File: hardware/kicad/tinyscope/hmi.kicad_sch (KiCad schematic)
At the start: 51 parts, among them J8 Waveshare 16498

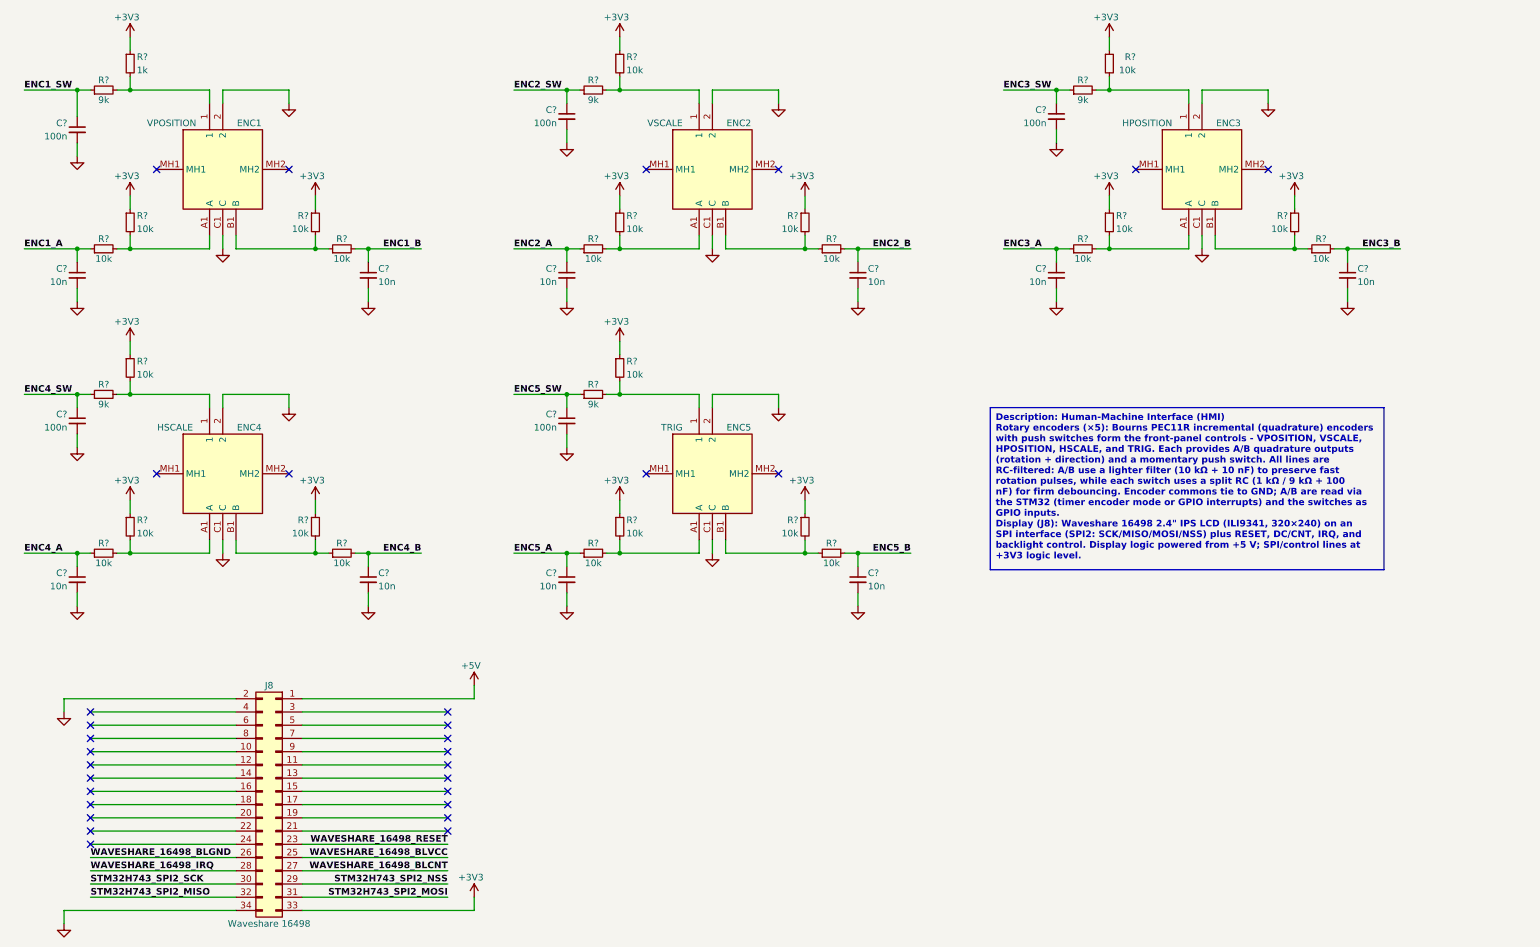
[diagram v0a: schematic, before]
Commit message: feat: hardware: Adds 6th encoder for display
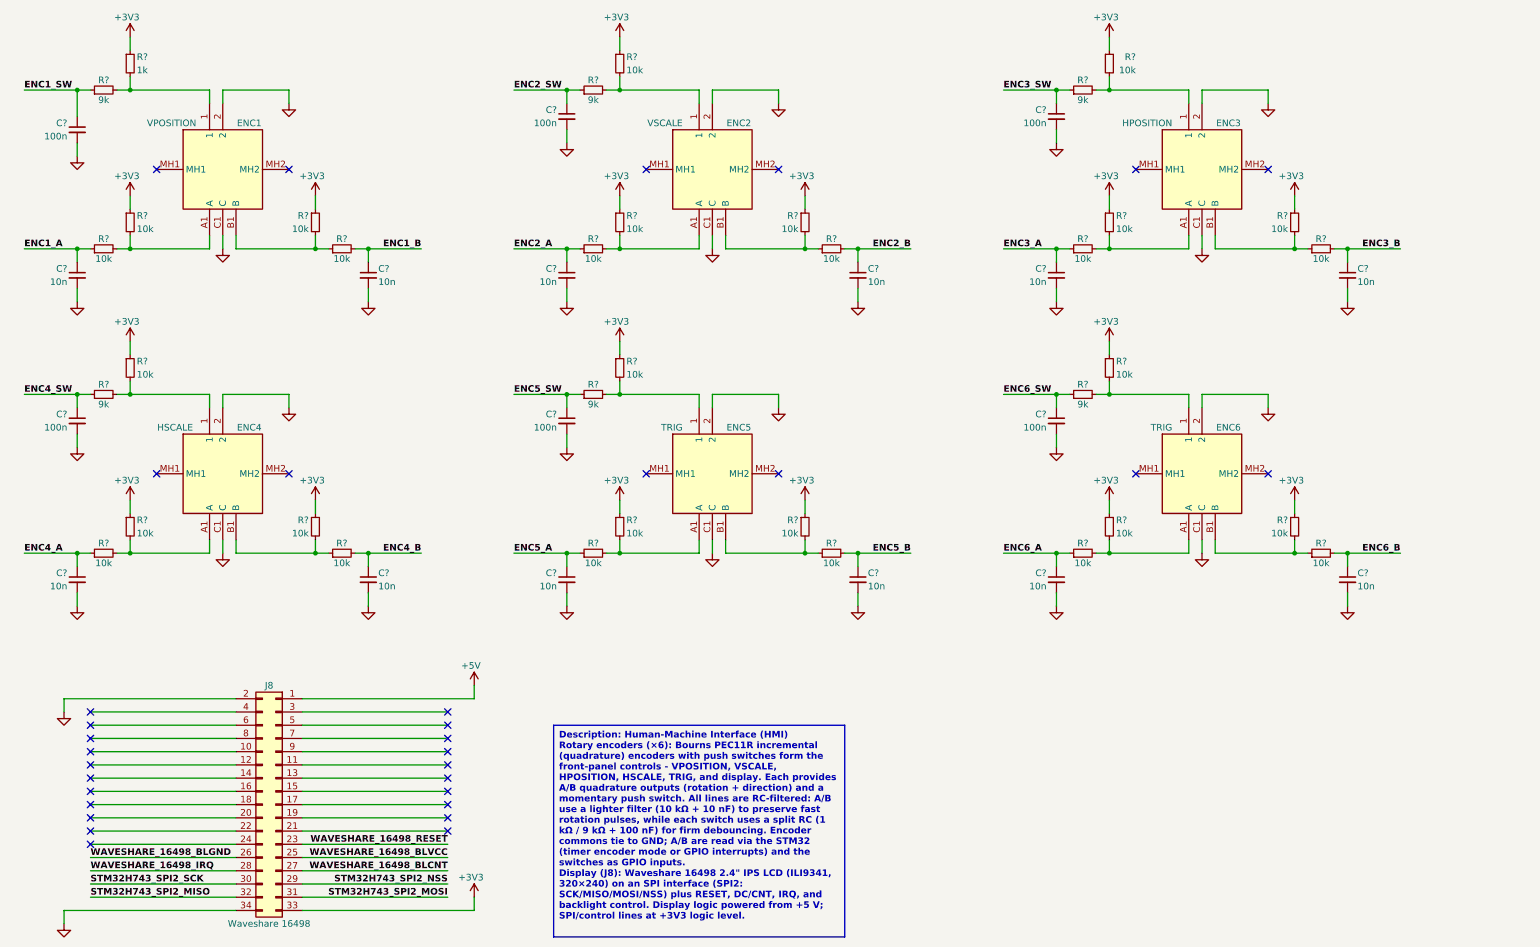
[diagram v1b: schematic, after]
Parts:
- added C?: 100n, symbol Device:C_Small
- added C? (x2): 10n, symbol Device:C_Small
- added ENC6: TRIG, PEC11R4220FS0024, symbol PEC11R-4220F-S0024:PEC11R-4220F-S0024
- added R? (x5): 10k, symbol Device:R_Small
- added R?: 9k, symbol Device:R_Small
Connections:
- net +3V3: now also R?.1, R?.1, R?.1
- net GND: now also C?.2, C?.2, C?.2, ENC6.2, ENC6.C1 (C)
- new net: ENC6.1, R?.2, R?.2
- new net: ENC6.A1 (A), R?.2, R?.2
- new net: ENC6.B1 (B), R?.1, R?.2
- new net ENC6_A: C?.1, R?.1
- new net ENC6_B: C?.1, R?.2
- new net ENC6_SW: C?.1, R?.1
- no-connect marks 31 -> 33

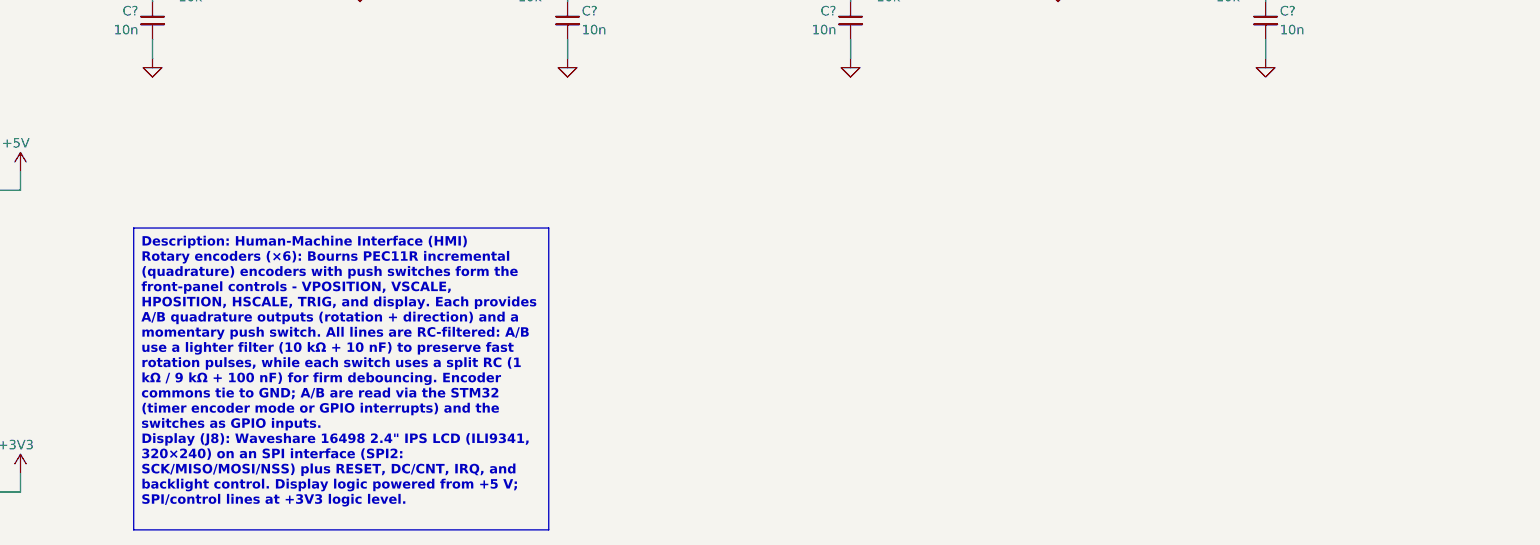
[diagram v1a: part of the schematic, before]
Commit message: feat: hardware: doc: Modifies placement for the schematic description
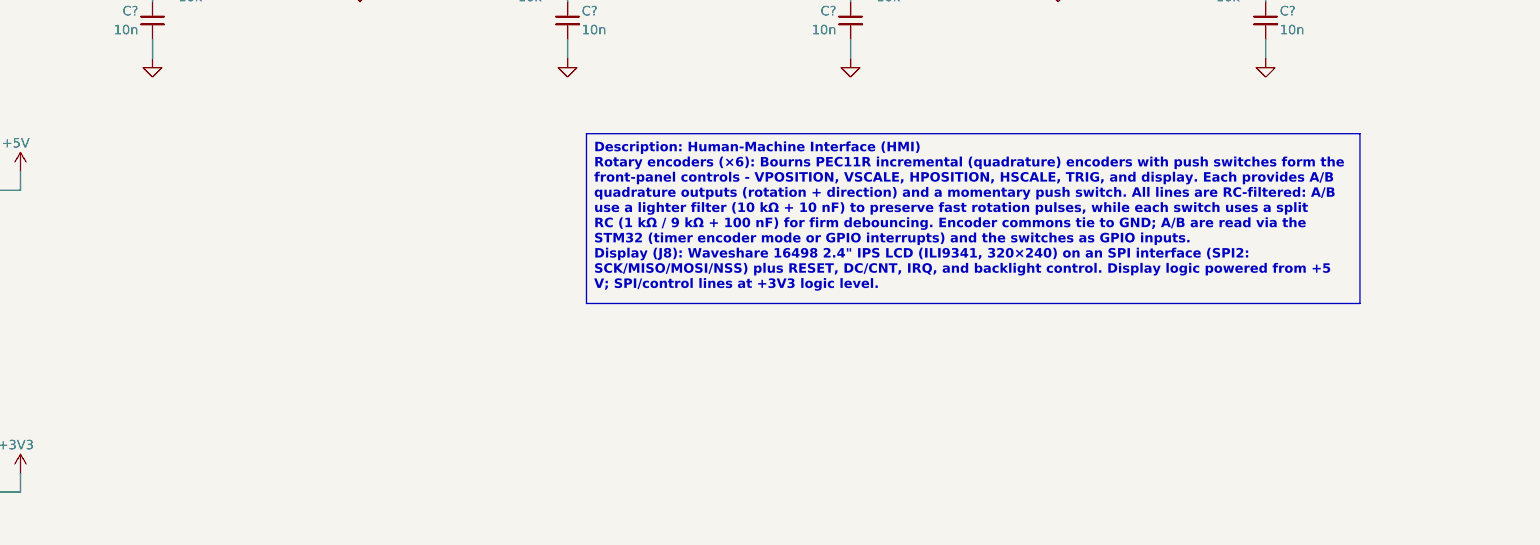
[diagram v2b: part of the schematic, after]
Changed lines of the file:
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@@
   )
   (text_box "Description: Human-Machine Interface (HMI)\nRotary encoders (×6): Bourns PEC11R incremental (quadrature) encoders with push switches form the front-panel controls - VPOSITION, VSCALE, HPOSITION, HSCALE, TRIG, and display. Each provides A/B quadrature outputs (rotation + direction) and a momentary push switch. All lines are RC-filtered: A/B use a lighter filter (10 kΩ + 10 nF) to preserve fast rotation pulses, while each switch uses a split RC (1 kΩ / 9 kΩ + 100 nF) for firm debouncing. Encoder commons tie to GND; A/B are read via the STM32 (timer encoder mode or GPIO interrupts) and the switches as GPIO inputs.\nDisplay (J8): Waveshare 16498 2.4\" IPS LCD (ILI9341, 320×240) on an SPI interface (SPI2: SCK/MISO/MOSI/NSS) plus RESET, DC/CNT, IRQ, and backlight control. Display logic powered from +5 V; SPI/control lines at +3V3 logic level."
-    (at 116.84 152.4 0) (size 55.88 40.64)
+    (at 177.8 139.7 0) (size 104.14 22.86)
     (stroke (width 0) (type default))
     (fill (type color) (color 255 255 194 1))

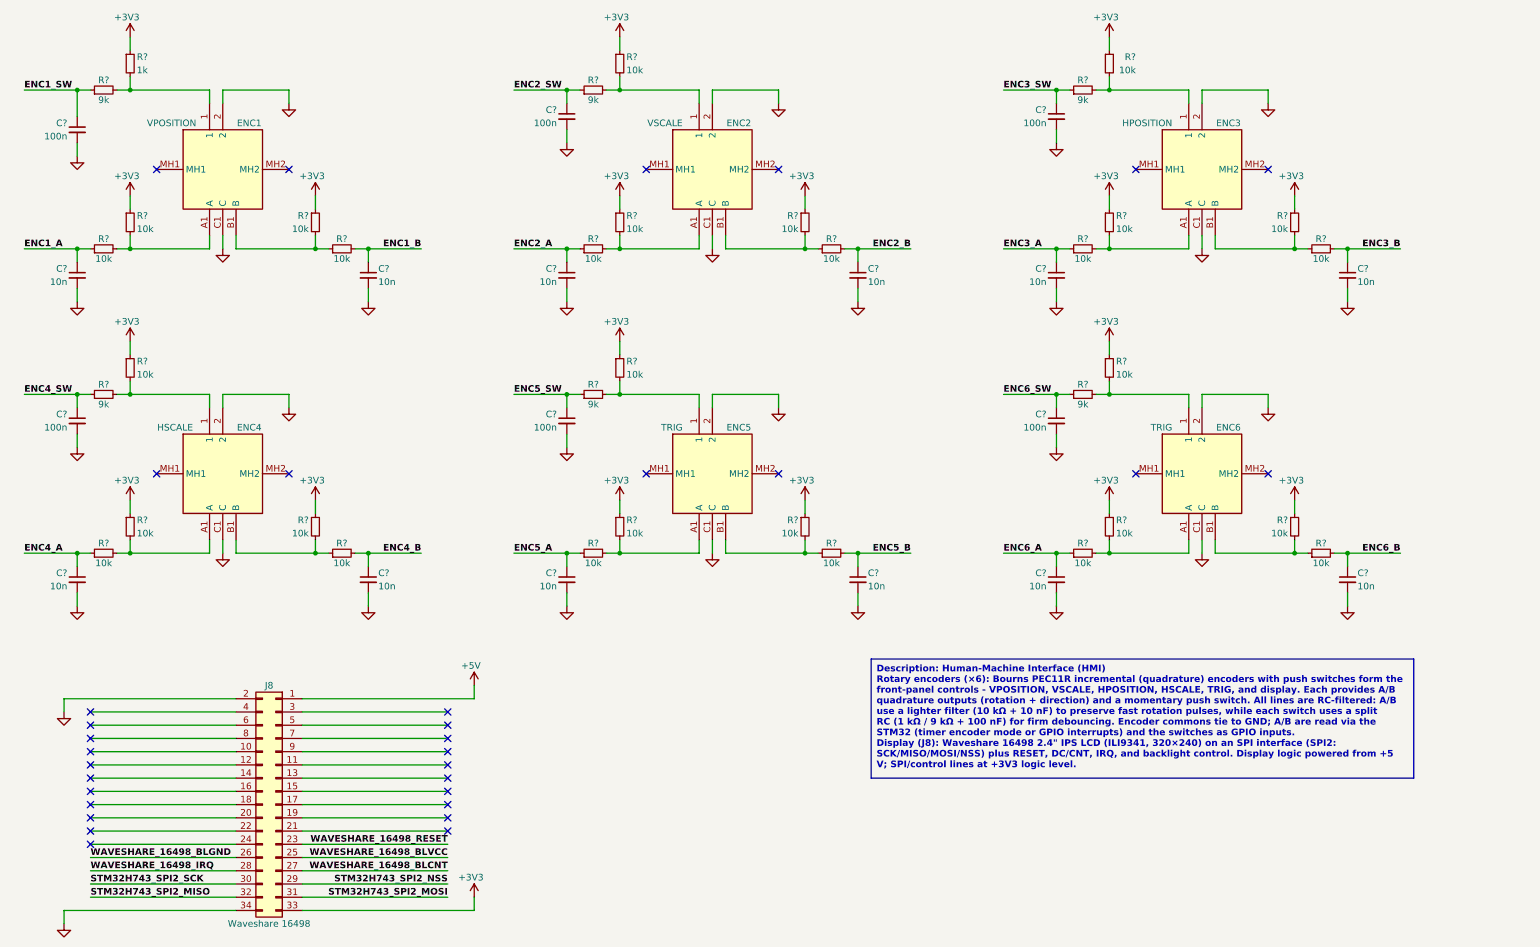
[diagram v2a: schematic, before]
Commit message: fix: hardware: Solves electrical rules warnings and errors #3
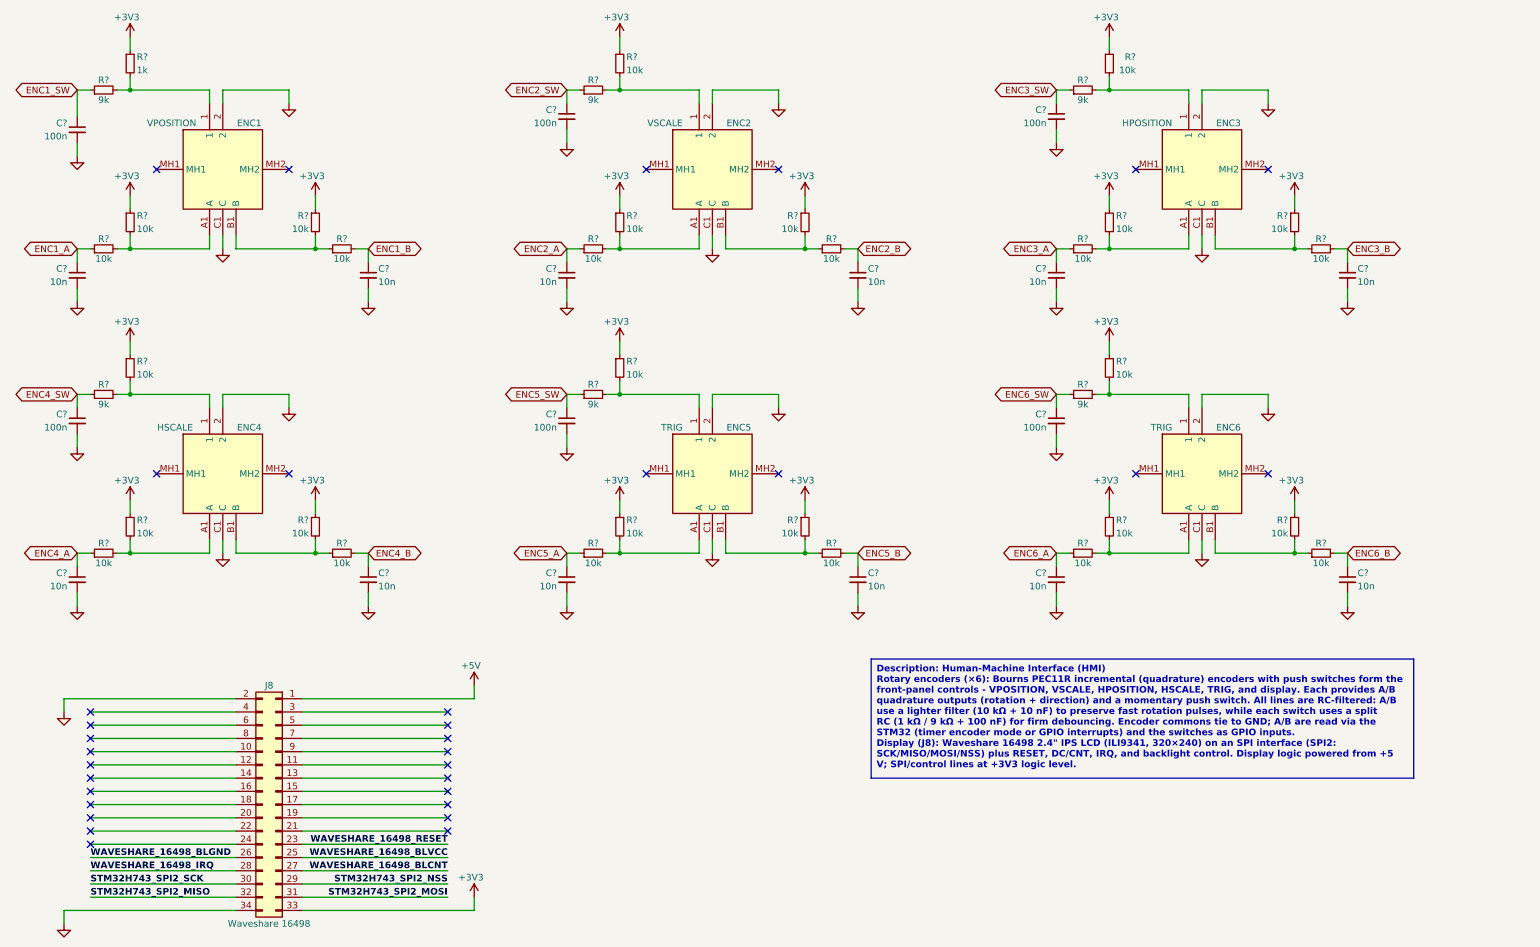
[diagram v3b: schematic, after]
